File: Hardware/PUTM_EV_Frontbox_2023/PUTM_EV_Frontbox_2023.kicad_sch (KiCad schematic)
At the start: 19 parts, among them J1 Conn_02x15_Counter_Clockwise, J3 STLINK-V3MINIE, U1 STM32G473RCTx

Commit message: Board review
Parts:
- H1, H2, H3, H4: footprint MountingHole:MountingHole_3.2mm_M3_DIN965_Pad_TopBottom -> MountingHole:MountingHole_3.2mm_M3_Pad_Via
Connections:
- net IMU_CLK is gone; now on net Safety_control: U1.56 (PB3)
- net IMU_MISO: no longer names the net of U1.57 (PB4)
- net IMU_MOSI: no longer names the net of U1.58 (PB5)
- no-connect marks 8 -> 18
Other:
- note added: "Doać voltage reference do VREF. od igancego"
- note added: "dodac header do programowania stdc14"
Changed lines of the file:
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@@
   )
   (no_connect (at 124.46 129.54))
+  (no_connect (at 238.76 33.02))
+  (no_connect (at 203.2 53.34))
+  (no_connect (at 238.76 86.36))
   (no_connect (at 238.76 101.6))
   (no_connect (at 203.2 86.36))
-  (no_connect (at 203.2 30.48))
+  (no_connect (at 238.76 83.82))
+  (no_connect (at 203.2 55.88))
   (no_connect (at 203.2 91.44))
   (no_connect (at 203.2 88.9))
+  (no_connect (at 238.76 35.56))
+  (no_connect (at 203.2 48.26))
+  (no_connect (at 238.76 30.48))
+  (no_connect (at 203.2 60.96))
+  (no_connect (at 203.2 58.42))
   (no_connect (at 124.46 137.16))
   (no_connect (at 238.76 99.06))
+  (no_connect (at 238.76 50.8))
   (polyline (pts (xy 139.7 165.735) (xy 177.165 165.735))
     (stroke (width 0) (type dot))
@@
     (stroke (width 0) (type default))
   )
-  (wire (pts (xy 247.65 81.28) (xy 238.76 81.28))
-    (stroke (width 0) (type default))
-  )
   (wire (pts (xy 125.73 83.185) (xy 129.54 83.185))
     (stroke (width 0) (type default))
@@
     (stroke (width 0) (type default))
   )
-  (wire (pts (xy 248.285 86.36) (xy 238.76 86.36))
-    (stroke (width 0) (type default))
-  )
   (wire (pts (xy 253.365 104.14) (xy 238.76 104.14))
     (stroke (width 0) (type default))
@@
     (stroke (width 0) (type default))
   )
+  (wire (pts (xy 238.76 81.28) (xy 267.97 81.28))
+    (stroke (width 0) (type default))
+  )
   (wire (pts (xy 31.75 52.07) (xy 53.34 52.07))
     (stroke (width 0) (type default))
@@
     (stroke (width 0) (type default))
   )
-  (wire (pts (xy 203.2 43.18) (xy 195.58 43.18))
+  (wire (pts (xy 203.2 43.18) (xy 190.5 43.18))
     (stroke (width 0) (type default))
   )
@@
     (stroke (width 0) (type default))
   )
-  (wire (pts (xy 203.2 40.64) (xy 195.58 40.64))
+  (wire (pts (xy 203.2 40.64) (xy 190.5 40.64))
     (stroke (width 0) (type default))
   )
@@
     (stroke (width 0) (type default))
   )
-  (wire (pts (xy 248.285 83.82) (xy 238.76 83.82))
-    (stroke (width 0) (type default))
-  )
   (wire (pts (xy 238.76 60.96) (xy 248.285 60.96))
     (stroke (width 0) (type default))
@@
     (stroke (width 0) (type dot))
   )
-  (wire (pts (xy 203.2 35.56) (xy 195.58 35.56))
+  (wire (pts (xy 203.2 35.56) (xy 190.5 35.56))
     (stroke (width 0) (type default))
   )
@@
     (effects (font (size 2 2) (thickness 0.4) bold) (justify left bottom))
   )
+  (text "dodac header do programowania stdc14\n" (at 109.22 118.11 0)
+    (effects (font (size 1.27 1.27)) (justify left bottom))
+  )
+  (text "Doać voltage reference do VREF. od igancego\n" (at 163.83 25.4 0)
+    (effects (font (size 1.27 1.27)) (justify left bottom))
+  )
   (text "CAN Bus\n" (at 123.825 32.385 0)
     (effects (font (size 2 2) (thickness 0.4) bold) (justify left bottom))
@@
     (effects (font (size 1.27 1.27)) (justify right bottom))
   )
-  (label "Safety_control" (at 257.81 23.495 0) (fields_autoplaced)
-    (effects (font (size 1.27 1.27)) (justify left bottom))
-  )
   (label "APPS1_3V3" (at 109.855 21.59 0) (fields_autoplaced)
     (effects (font (size 1.27 1.27)) (justify left bottom))
@@
     (effects (font (size 1.27 1.27)) (justify right bottom))
   )
-  (label "NRST" (at 195.58 35.56 180) (fields_autoplaced)
-    (effects (font (size 1.27 1.27)) (justify right bottom))
+  (label "NRST" (at 190.5 35.56 0) (fields_autoplaced)
+    (effects (font (size 1.27 1.27)) (justify left bottom))
   )
   (label "SUSPENSION_POT2_IN" (at 33.02 39.37 0) (fields_autoplaced)
@@
     (effects (font (size 1.27 1.27)) (justify right bottom))
   )
-  (label "HSE_OUT" (at 195.58 43.18 180) (fields_autoplaced)
-    (effects (font (size 1.27 1.27)) (justify right bottom))
+  (label "HSE_OUT" (at 190.5 43.18 0) (fields_autoplaced)
+    (effects (font (size 1.27 1.27)) (justify left bottom))
   )
   (label "CAN2-" (at 110.49 52.705 0) (fields_autoplaced)
@@
     (effects (font (size 1.27 1.27)) (justify right bottom))
   )
-  (label "IMU_MISO" (at 248.285 83.82 180) (fields_autoplaced)
-    (effects (font (size 1.27 1.27)) (justify right bottom))
-  )
   (label "APPS1_3V3" (at 15.24 54.61 0) (fields_autoplaced)
     (effects (font (size 1.27 1.27)) (justify left bottom))
@@
     (effects (font (size 1.27 1.27)) (justify left bottom))
   )
-  (label "IMU_MOSI" (at 248.285 86.36 180) (fields_autoplaced)
-    (effects (font (size 1.27 1.27)) (justify right bottom))
-  )
   (label "DEBUG_LED3" (at 252.73 111.76 180) (fields_autoplaced)
     (effects (font (size 1.27 1.27)) (justify right bottom))
@@
     (effects (font (size 1.27 1.27)) (justify left bottom))
   )
-  (label "IMU_CLK" (at 247.65 81.28 180) (fields_autoplaced)
-    (effects (font (size 1.27 1.27)) (justify right bottom))
-  )
   (label "OVERTRAVEL" (at 33.02 62.23 0) (fields_autoplaced)
     (effects (font (size 1.27 1.27)) (justify left bottom))
@@
     (effects (font (size 1.27 1.27)) (justify left bottom))
   )
-  (label "HSE_IN" (at 195.58 40.64 180) (fields_autoplaced)
-    (effects (font (size 1.27 1.27)) (justify right bottom))
+  (label "HSE_IN" (at 190.5 40.64 0) (fields_autoplaced)
+    (effects (font (size 1.27 1.27)) (justify left bottom))
   )
   (label "DEBUG_LED4" (at 139.065 103.505 0) (fields_autoplaced)
@@
   (label "STEERING_POSITION_IN" (at 33.02 36.83 0) (fields_autoplaced)
     (effects (font (size 1.27 1.27)) (justify left bottom))
+  )
+  (label "Safety_control" (at 267.97 81.28 180) (fields_autoplaced)
+    (effects (font (size 1.27 1.27)) (justify right bottom))
   )
   (symbol (lib_id "power:+3.3V") (at 117.475 81.28 0) (unit 1)
@@
       (effects (font (size 1.27 1.27)) (justify left))
     )
-    (property "Footprint" "MountingHole:MountingHole_3.2mm_M3_DIN965_Pad_TopBottom" (at 236.855 158.115 0)
+    (property "Footprint" "MountingHole:MountingHole_3.2mm_M3_Pad_Via" (at 236.855 158.115 0)
       (effects (font (size 1.27 1.27)) hide)
     )
@@
       (effects (font (size 1.27 1.27)) (justify left))
     )
-    (property "Footprint" "MountingHole:MountingHole_3.2mm_M3_DIN965_Pad_TopBottom" (at 260.35 146.05 0)
+    (property "Footprint" "MountingHole:MountingHole_3.2mm_M3_Pad_Via" (at 260.35 146.05 0)
       (effects (font (size 1.27 1.27)) hide)
     )
@@
       (effects (font (size 1.27 1.27)) (justify left))
     )
-    (property "Footprint" "MountingHole:MountingHole_3.2mm_M3_DIN965_Pad_TopBottom" (at 260.35 158.115 0)
+    (property "Footprint" "MountingHole:MountingHole_3.2mm_M3_Pad_Via" (at 260.35 158.115 0)
       (effects (font (size 1.27 1.27)) hide)
     )
@@
       (effects (font (size 1.27 1.27)) (justify left))
     )
-    (property "Footprint" "MountingHole:MountingHole_3.2mm_M3_DIN965_Pad_TopBottom" (at 236.855 146.05 0)
-      (effects (font (size 1.27 1.27)) hide)
-    )
+    (property "Footprint" "MountingHole:MountingHole_3.2mm_M3_Pad_Via" (at 236.855 146.05 0)
+      (effects (font (size 1.27 1.27)) hide)
+    )

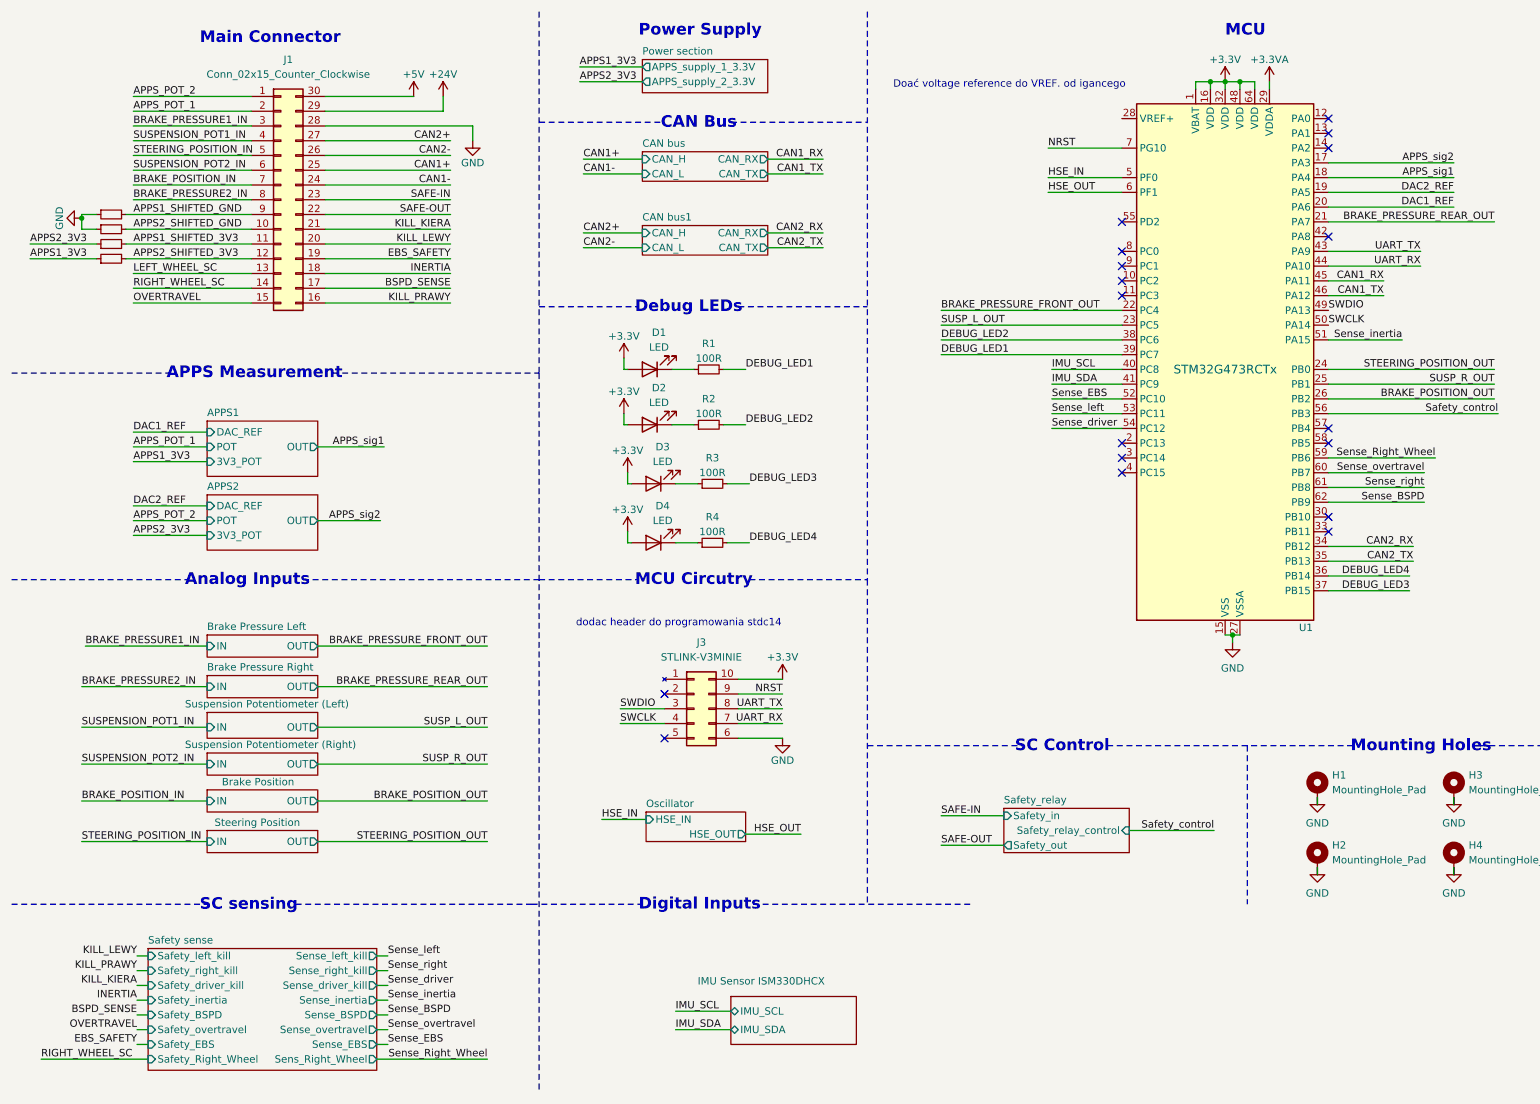
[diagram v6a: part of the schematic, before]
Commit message: Moved sw cap closer to pins
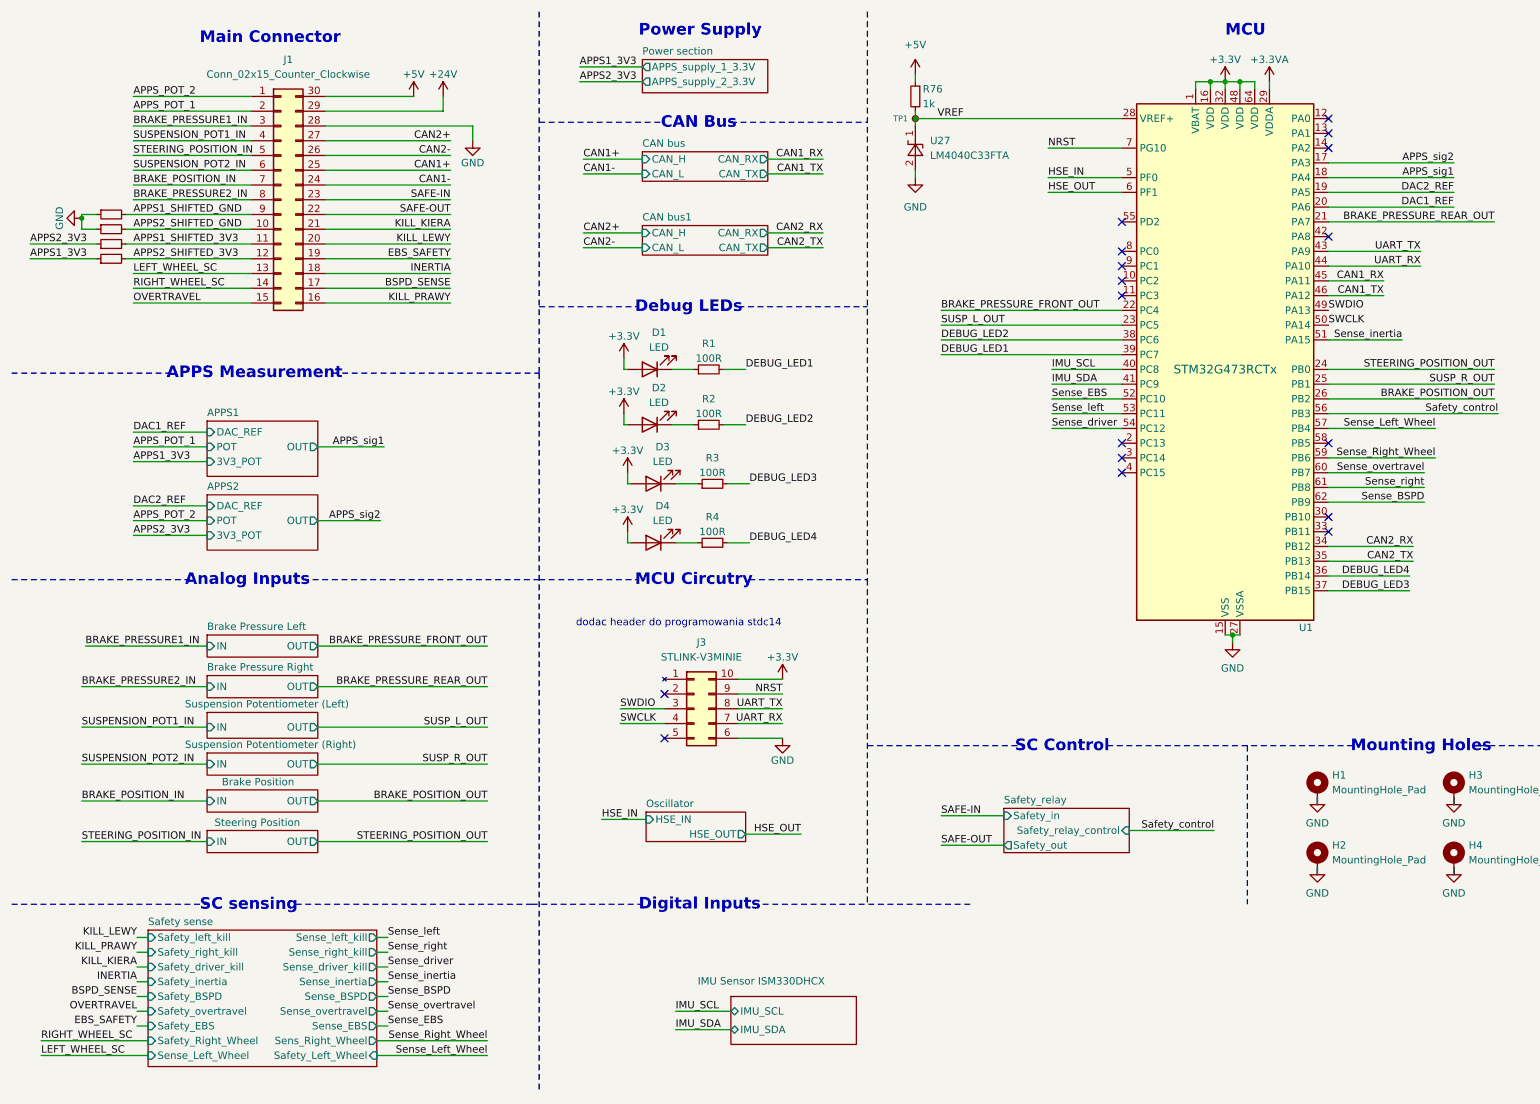
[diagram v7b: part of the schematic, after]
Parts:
- added R76: 1k, Resistor_SMD:R_0603_1608Metric, symbol Device:R_Small
- added TP1: TestPoint_Small, TestPoint:TestPoint_Pad_D1.0mm, symbol Connector:TestPoint_Small
- added U27: LM4040C33FTA, Package_TO_SOT_SMD:SOT-23, symbol LM4040:LM4040
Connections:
- net +5V: now also R76.1
- net GND: now also U27.2 (A)
- net VREF: now reaches U1.28 (VREF+)
- net VREF: now also R76.2, TP1.1, U27.1 (K)
- net Sense_Left_Wheel: now reaches U1.57 (PB4)
- no-connect marks 18 -> 17
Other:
- sheet Safety sense ports: added Safety_Left_Wheel, Sense_Left_Wheel; removed none
- note removed: "Doać voltage reference do VREF. od igancego"

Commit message: New firmware
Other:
- note added: "Dodać dodatkowe pomiary temperatury przekładni"
- note added: "Dodać programator stlink v3 mini"
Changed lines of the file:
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@@
     (effects (font (size 2 2) (thickness 0.4) bold) (justify left bottom))
+  )
+  (text "Dodać programator stlink v3 mini\n" (at 298.45 9.525 0)
+    (effects (font (size 3 3)) (justify left bottom))
   )
   (text "MCU Circutry\n\n" (at 119.38 114.3 0)
@@
     (effects (font (size 2 2) (thickness 0.4) bold) (justify left bottom))
   )
+  (text "Dodać dodatkowe pomiary temperatury przekładni" (at 298.45 4.445 0)
+    (effects (font (size 3 3)) (justify left bottom))
+  )
   (text "SC Control\n" (at 184.785 139.7 0)
